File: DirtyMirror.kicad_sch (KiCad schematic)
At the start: 72 parts, among them J101 PWR, J102 ScopeGroundLoop, SW101 SW_SPDT, U101 TL074, U102 TL074

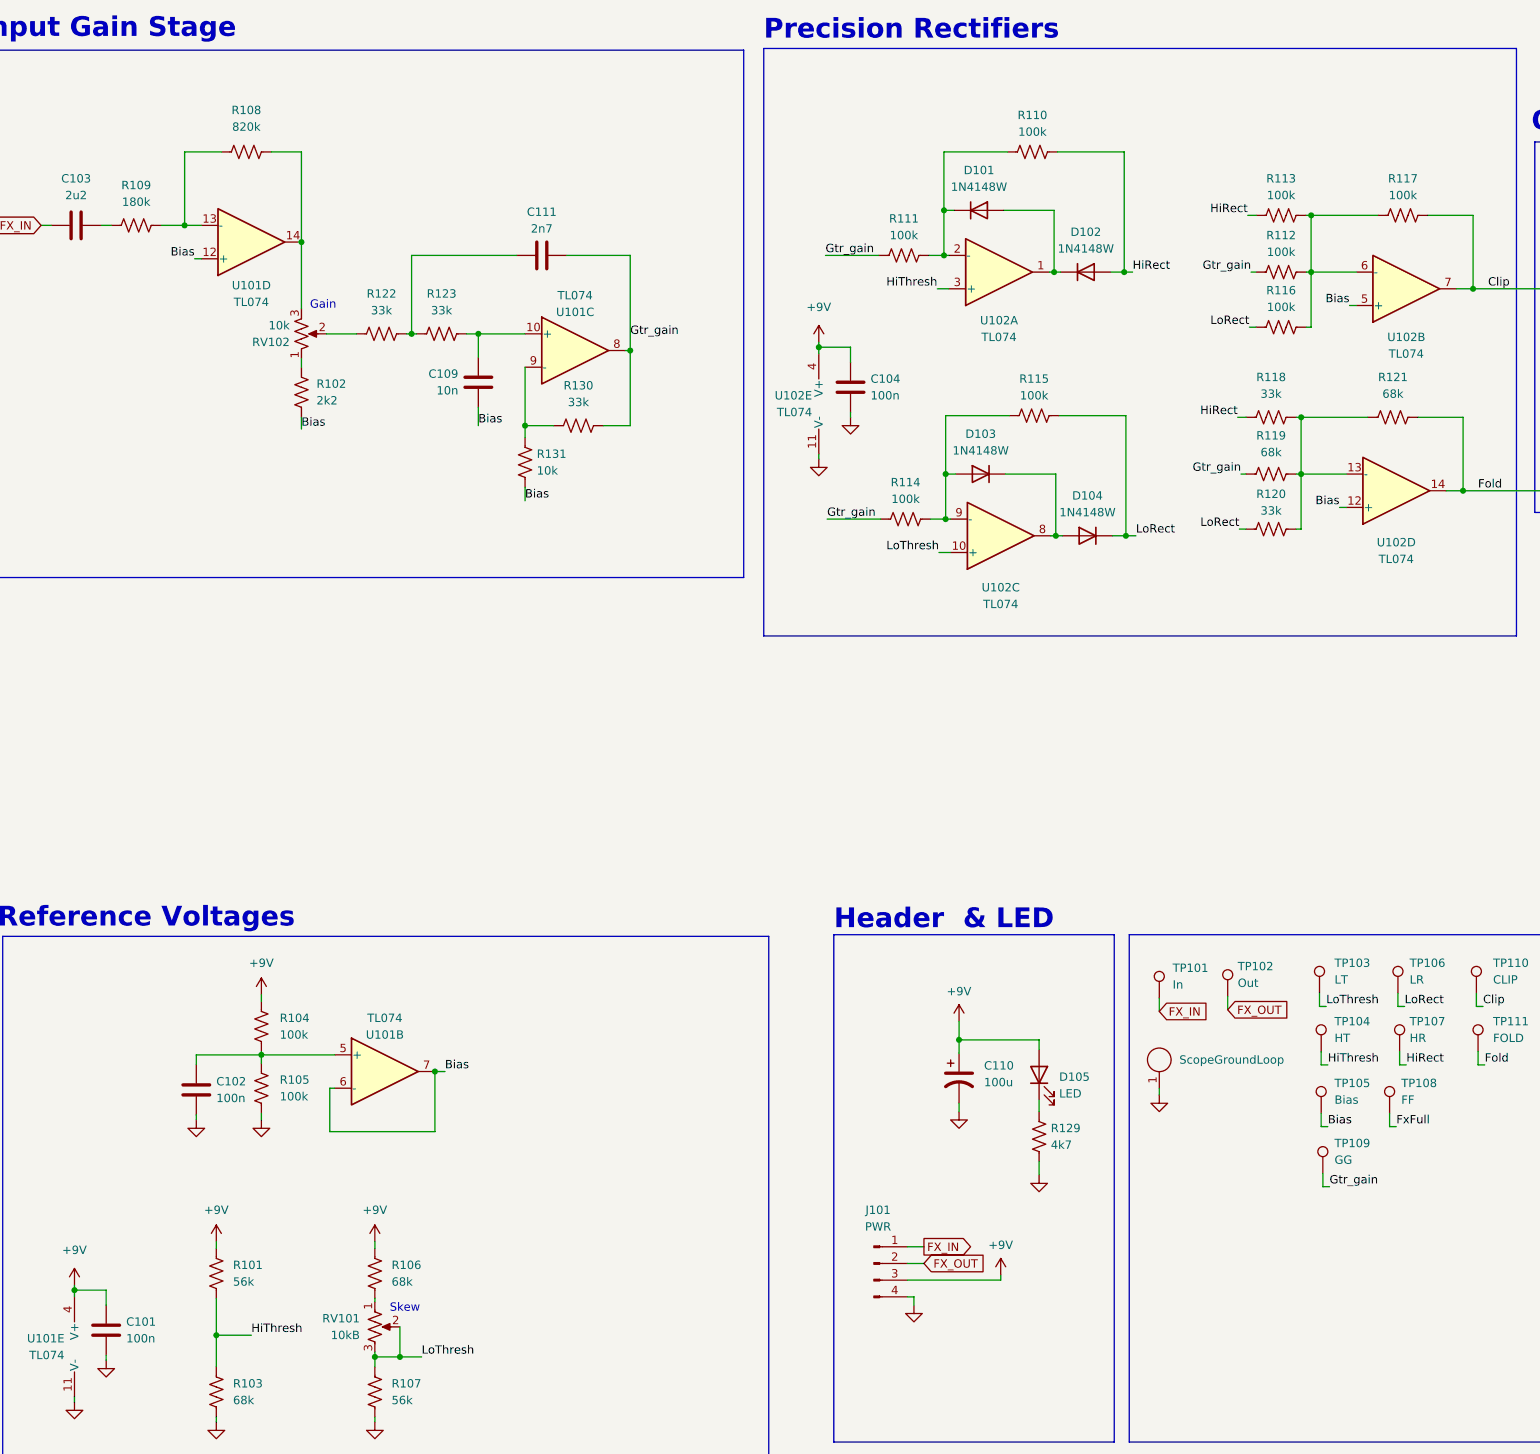
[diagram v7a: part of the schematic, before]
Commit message: summing amp tweaks
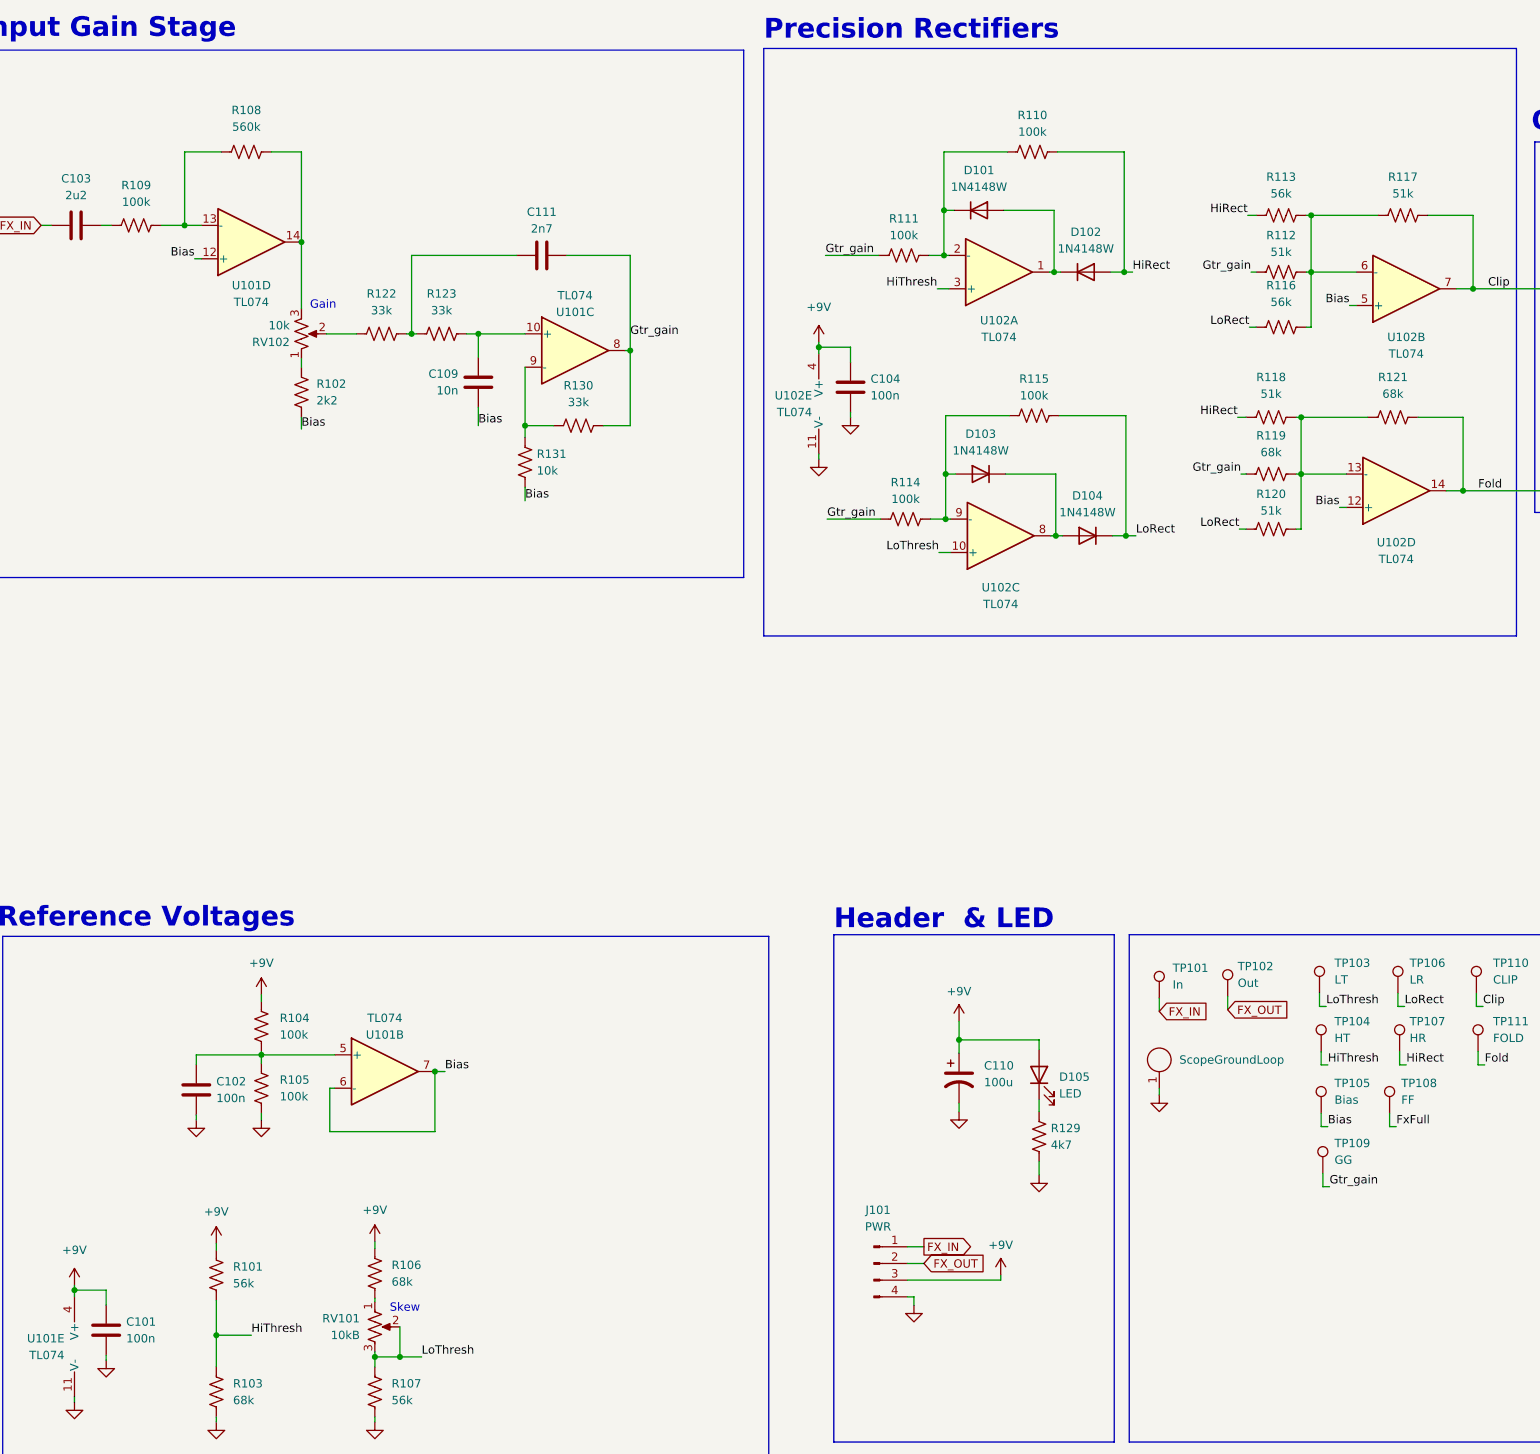
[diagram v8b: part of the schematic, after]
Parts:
- R108: value 820k -> 560k
- R109: value 180k -> 100k
- R112, R117: value 100k -> 51k
- R113, R116: value 100k -> 56k
- R118, R120: value 33k -> 51k
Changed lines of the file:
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@@
 	(wire
 		(pts
-			(xy 49.53 221.488) (xy 49.53 227.076)
+			(xy 49.53 221.742) (xy 49.53 227.076)
 		)
 		(stroke
@@
 	(wire
 		(pts
-			(xy 49.53 212.852) (xy 49.53 213.868)
+			(xy 49.53 213.106) (xy 49.53 214.122)
 		)
 		(stroke
@@
 		(fields_autoplaced yes)
 		(property "Reference" "R116"
-			(at 211.582 68.072 90)
+			(at 211.582 67.31 90)
 			(effects
 				(font
@@
 			)
 		)
-		(property "Value" "100k"
-			(at 211.582 70.612 90)
+		(property "Value" "56k"
+			(at 211.582 69.85 90)
 			(effects
 				(font
@@
 		(fields_autoplaced yes)
 		(property "Reference" "R113"
-			(at 211.582 51.054 90)
+			(at 211.582 50.8 90)
 			(effects
 				(font
@@
 			)
 		)
-		(property "Value" "100k"
-			(at 211.582 53.594 90)
+		(property "Value" "56k"
+			(at 211.582 53.34 90)
 			(effects
 				(font
@@
 			)
 		)
-		(property "Value" "100k"
+		(property "Value" "51k"
 			(at 211.582 62.23 90)
 			(effects
@@
 	(symbol
 		(lib_id "power:+9V")
-		(at 49.53 212.852 0)
+		(at 49.53 213.106 0)
 		(unit 1)
 		(exclude_from_sim no)
@@
 		(fields_autoplaced yes)
 		(property "Reference" "#PWR0104"
-			(at 49.53 216.662 0)
+			(at 49.53 216.916 0)
 			(effects
 				(font
@@
 		)
 		(property "Value" "+9V"
-			(at 49.53 208.026 0)
+			(at 49.53 208.28 0)
 			(effects
 				(font
@@
 		)
 		(property "Footprint" ""
-			(at 49.53 212.852 0)
+			(at 49.53 213.106 0)
 			(effects
 				(font
@@
 		)
 		(property "Datasheet" ""
-			(at 49.53 212.852 0)
+			(at 49.53 213.106 0)
 			(effects
 				(font
@@
 		)
 		(property "Description" "Power symbol creates a global label with name \"+9V\""
-			(at 49.53 212.852 0)
+			(at 49.53 213.106 0)
 			(effects
 				(font
@@
 			)
 		)
-		(property "Value" "180k"
+		(property "Value" "100k"
 			(at 37.338 54.61 90)
 			(effects
@@
 			)
 		)
-		(property "Value" "33k"
+		(property "Value" "51k"
 			(at 210.058 101.6 90)
 			(effects
@@
 			)
 		)
-		(property "Value" "33k"
+		(property "Value" "51k"
 			(at 210.058 83.82 90)
 			(effects
@@
 			)
 		)
-		(property "Value" "820k"
+		(property "Value" "560k"
 			(at 54.102 43.18 90)
 			(effects
@@
 	(symbol
 		(lib_id "Device:R_US")
-		(at 49.53 217.678 0)
+		(at 49.53 217.932 0)
 		(unit 1)
 		(exclude_from_sim no)
@@
 		(fields_autoplaced yes)
 		(property "Reference" "R101"
-			(at 52.07 216.4079 0)
+			(at 52.07 216.6619 0)
 			(effects
 				(font
@@
 		)
 		(property "Value" "56k"
-			(at 52.07 218.9479 0)
+			(at 52.07 219.2019 0)
 			(effects
 				(font
@@
 		)
 		(property "Footprint" "Resistor_SMD:R_0805_2012Metric"
-			(at 50.546 217.932 90)
+			(at 50.546 218.186 90)
 			(effects
 				(font
@@
 		)
 		(property "Datasheet" "~"
-			(at 49.53 217.678 0)
+			(at 49.53 217.932 0)
 			(effects
 				(font
@@
 		)
 		(property "Description" "Resistor, US symbol"
-			(at 49.53 217.678 0)
+			(at 49.53 217.932 0)
 			(effects
 				(font
@@
 		(fields_autoplaced yes)
 		(property "Reference" "R117"
-			(at 230.124 51.054 90)
+			(at 230.124 50.8 90)
 			(effects
 				(font
@@
 			)
 		)
-		(property "Value" "100k"
-			(at 230.124 53.594 90)
+		(property "Value" "51k"
+			(at 230.124 53.34 90)
 			(effects
 				(font
